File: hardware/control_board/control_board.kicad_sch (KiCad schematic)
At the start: 0 parts

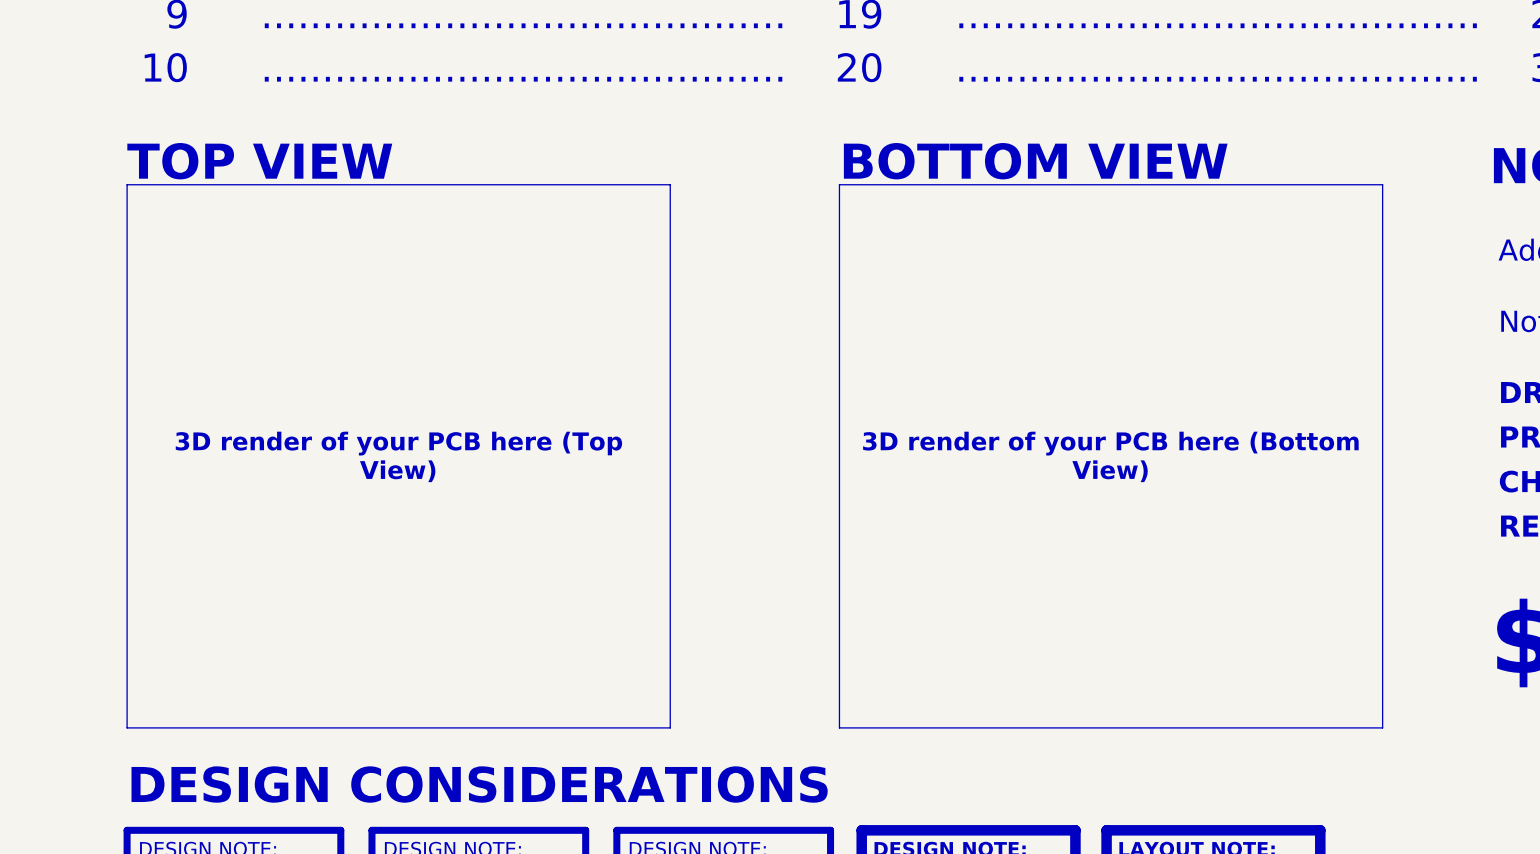
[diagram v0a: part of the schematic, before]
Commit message: Tweaking existing gerber files and schematics to comply with new project structure
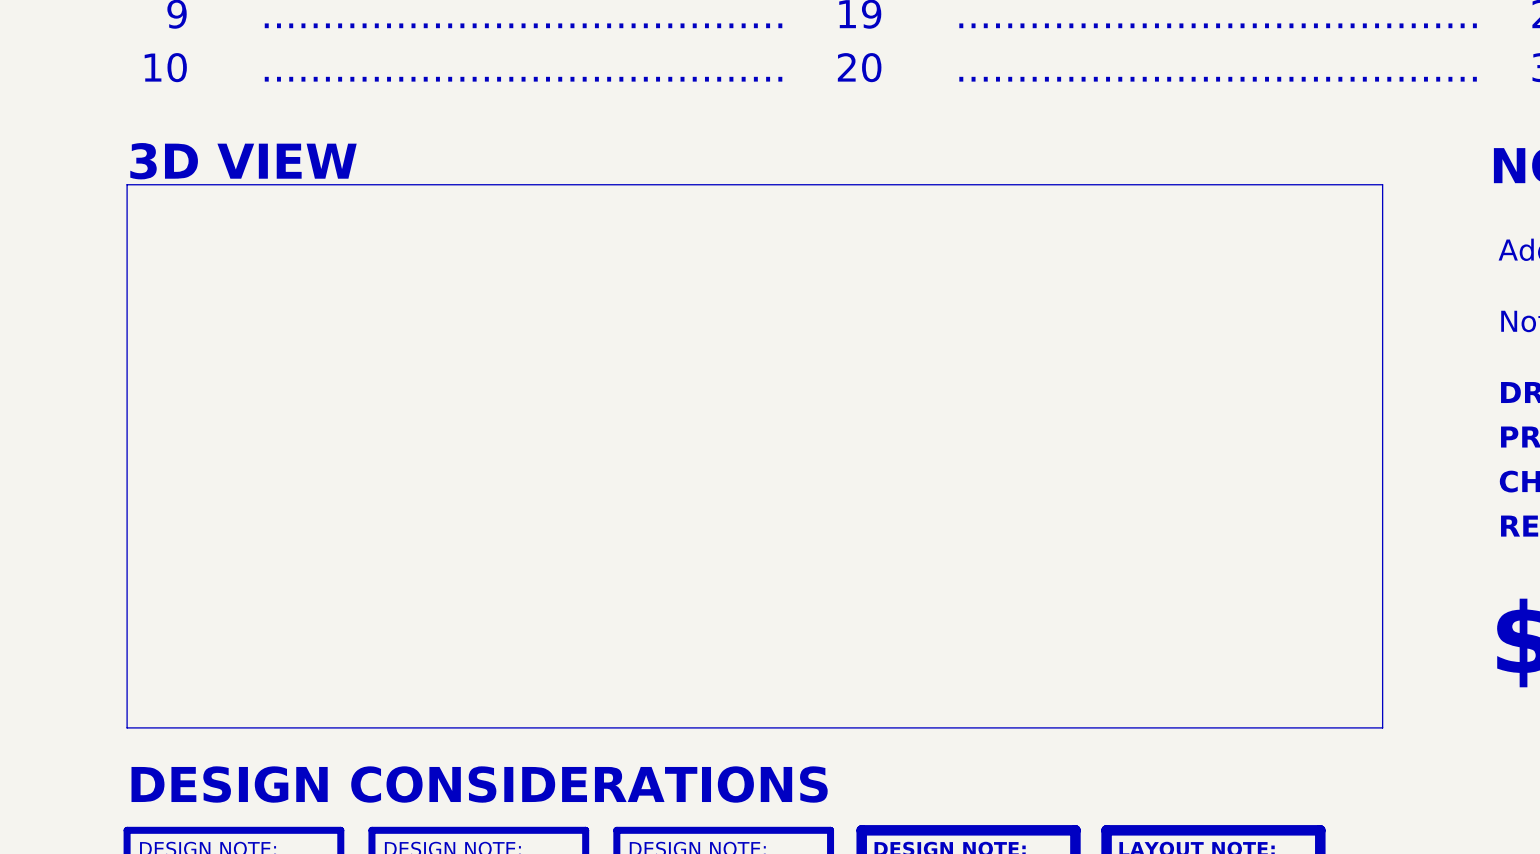
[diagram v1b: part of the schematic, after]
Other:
- note added: "3D VIEW"
- note removed: "BOTTOM VIEW"
- note removed: "TOP VIEW"
